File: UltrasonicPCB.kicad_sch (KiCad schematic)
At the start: 13 parts, among them J7 Conn_01x10

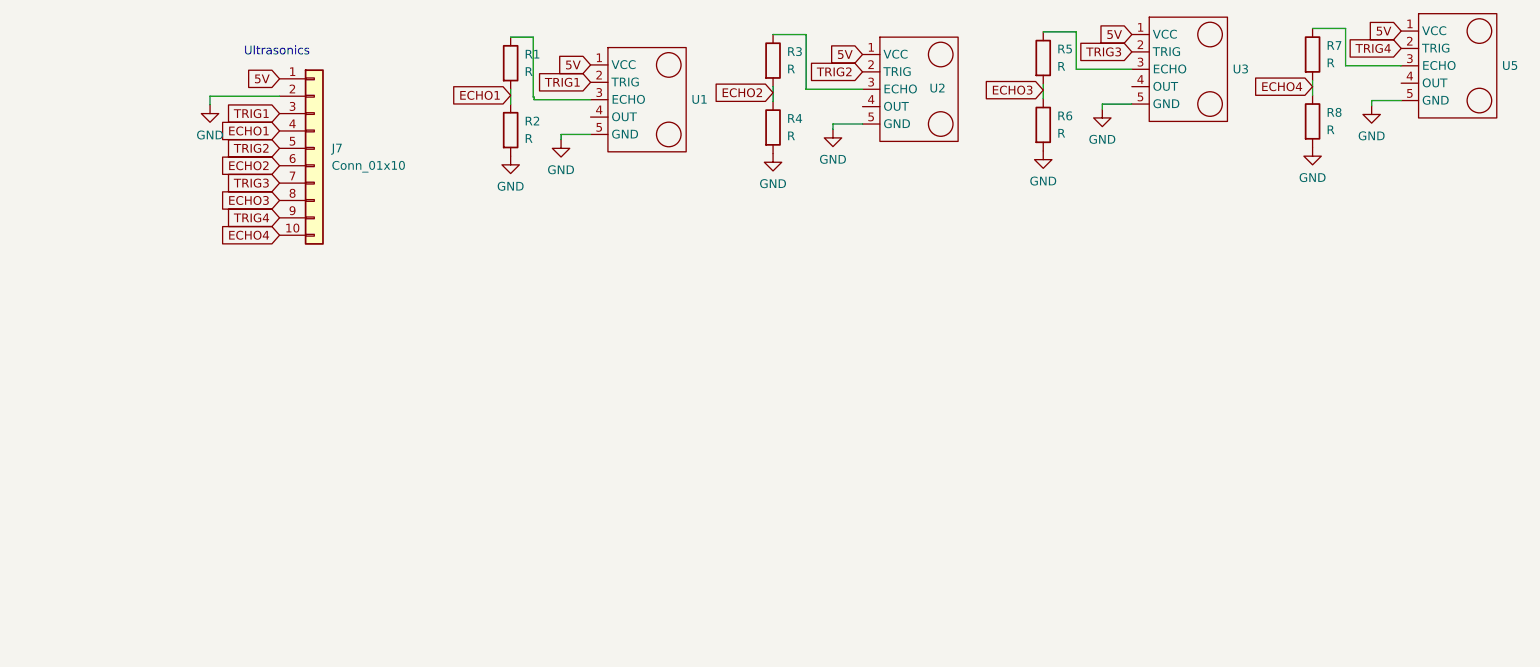
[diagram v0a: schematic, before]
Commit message: Updated with 1 echo
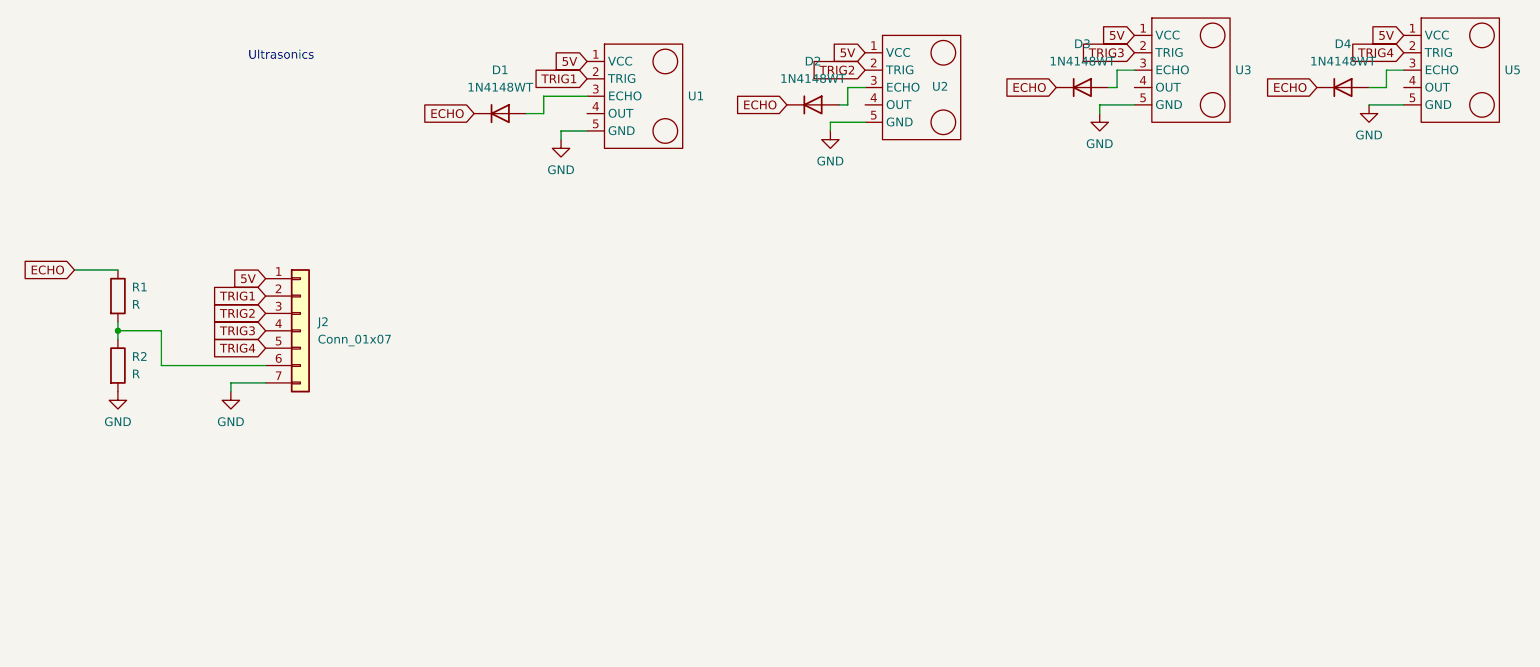
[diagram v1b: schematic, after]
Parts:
- removed J7: Conn_01x10, Connector_IDC:IDC-Header_2x05_P2.54mm_Vertical, symbol Connector_Generic:Conn_01x10
- removed R3, R4, R5, R6, R7, R8: R, Resistor_SMD:R_0805_2012Metric_Pad1.20x1.40mm_HandSolder, symbol Device:R
- added D1, D2, D3, D4: 1N4148WT, Diode_SMD:D_SOD-123, symbol Diode:1N4148WT
- added J2: Conn_01x07, Connector_IDC:IDC-Header_2x04_P2.54mm_Vertical, symbol Connector_Generic:Conn_01x07
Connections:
- net 5V: now also J2.1 (Pin_1)
- net GND: now also J2.7 (Pin_7)
- net TRIG1: now also J2.2 (Pin_2)
- net TRIG2: now also J2.3 (Pin_3)
- net TRIG3: now also J2.4 (Pin_4)
- net TRIG4: now also J2.5 (Pin_5)
- net at U3.3 (ECHO): now also D3.2 (A)
- net at U5.3 (ECHO): now also D4.2 (A)
- net at U2.3 (ECHO): now also D2.2 (A)
- net at U1.3 (ECHO): now also D1.2 (A); no longer R1.1
- net ECHO1: no longer names the net of R1.2, R2.1
- net ECHO1: now also J2.6 (Pin_6)
- new net ECHO: D1.1 (K), D2.1 (K), D3.1 (K), D4.1 (K), R1.1
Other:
- moved on the sheet: R1, R2, U1, U5

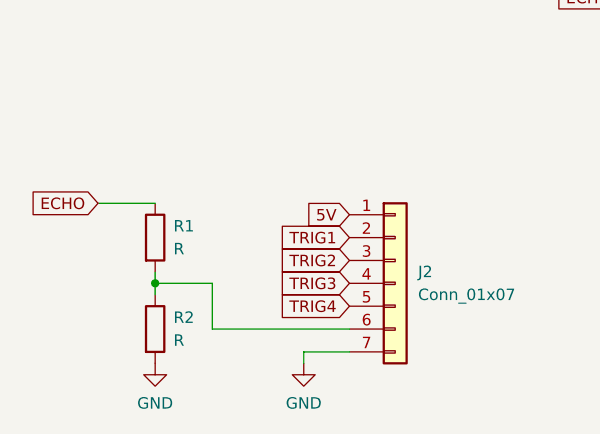
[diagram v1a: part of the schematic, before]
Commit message: Changed Outline
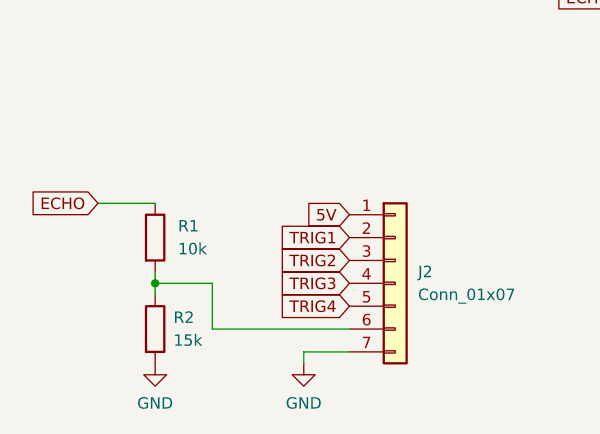
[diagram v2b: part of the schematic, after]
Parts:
- R1: value R -> 10k
- R2: value R -> 15k
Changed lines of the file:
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@@
 		(fields_autoplaced yes)
 		(property "Reference" "R1"
-			(at 42.672 87.63 0)
+			(at 43.18 87.6299 0)
 			(effects
 				(font
@@
 			)
 		)
-		(property "Value" "R"
-			(at 42.672 90.17 0)
+		(property "Value" "10k"
+			(at 43.18 90.1699 0)
 			(effects
 				(font
@@
 			)
 		)
-		(property "Value" "R"
+		(property "Value" "15k"
 			(at 42.672 100.33 0)
 			(effects

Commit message: Remake the PCB
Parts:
- added H1, H2, H3, H4, H5, H6, H7, H8: MountingHole, MountingHole:MountingHole_3.2mm_M3_DIN965_Pad, symbol Mechanical:MountingHole
